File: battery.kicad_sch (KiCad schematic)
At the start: 1 part, among them J2 Screw_Terminal_01x02

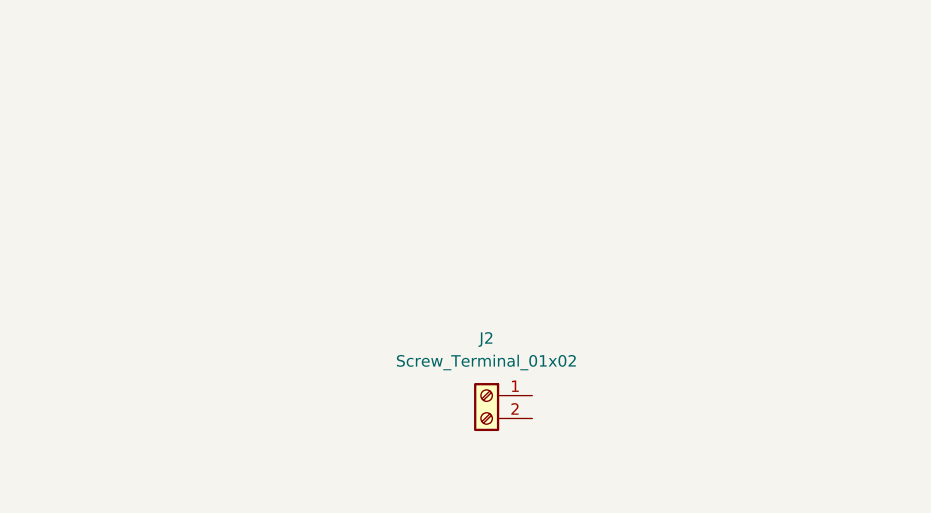
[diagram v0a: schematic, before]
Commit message: Started working on the audio input, including a rough-draft of the first stage.
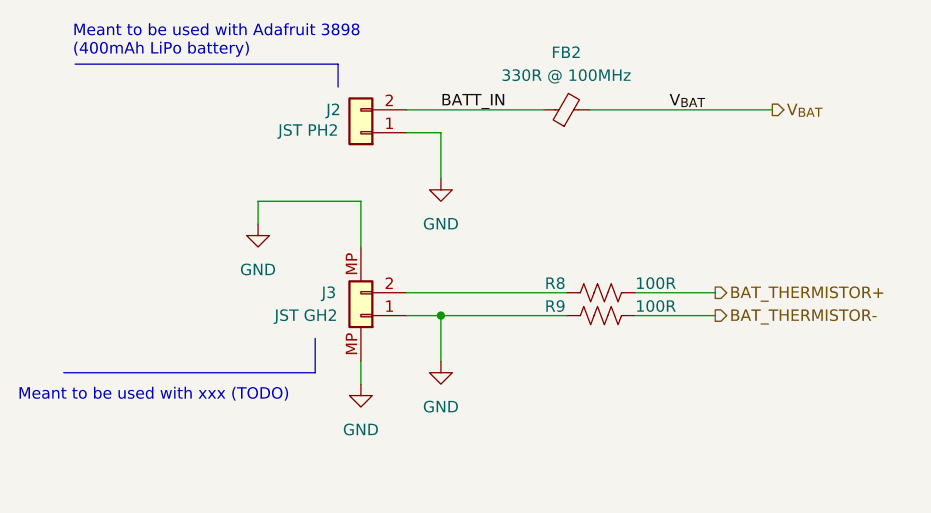
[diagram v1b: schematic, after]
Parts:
- removed J2: Screw_Terminal_01x02, Connector_JST:JST_PH_S2B-PH-SM4-TB_1x02-1MP_P2.00mm_Horizontal, symbol Connector:Screw_Terminal_01x02
- added FB2: 330R @ 100MHz, Inductor_SMD:L_0402_1005Metric, symbol #inventree_kicad:FB_330R_0402_1A2
- added J2: JST PH2, Connector_JST:JST_PH_S2B-PH-K_1x02_P2.00mm_Horizontal, symbol #inventree_kicad:PWR_CONN_2PIN_JST_PH2_RA_THRU
- added J3: JST GH2, Connector_JST:JST_GH_SM02B-GHS-TB_1x02-1MP_P1.25mm_Horizontal, symbol #inventree_kicad:SIG_CONN_2PIN_JST_GH2_RA_SMD
- added R8, R9: 100R, Resistor_SMD:R_0402_1005Metric, symbol #inventree_kicad:R_100R_0402_1PCT_0W0625
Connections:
- new net: J3.2 (Pin_2), R8.1
- new net BATT_IN: FB2.1, J2.2 (Pin_2)
- new net BAT_THERMISTOR+: R8.2
- new net BAT_THERMISTOR-: R9.2
- new net GND: J2.1 (Pin_1), J3.1 (Pin_1), J3.MP, R9.1
- new net V_{BAT}: FB2.2
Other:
- note added: "Meant to be used with Adafruit 3898 (400mAh LiPo battery)"
- note added: "Meant to be used with xxx (TODO)"

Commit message: Implemented boost stage and now working on schematics for current buffers and rail splitter.
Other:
- title: (none) -> ${PROJECT_NAME}
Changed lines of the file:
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@@
 	(generator_version "10.0")
 	(paper "A4")
+	(title_block
+		(title "${PROJECT_NAME}")
+		(date "2026-08-25")
+		(rev "${REVISION}")
+		(comment 1 "${PCBA_IPN}")
+	)
 	(text "Meant to be used with xxx (TODO)"
 		(exclude_from_sim no)

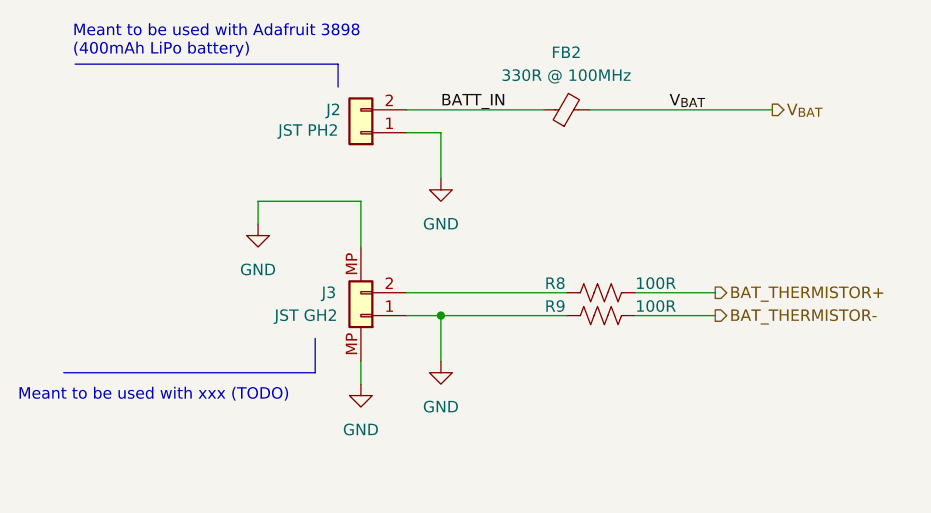
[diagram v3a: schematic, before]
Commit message: Preliminary layout complete, done on airpane so needs verification.
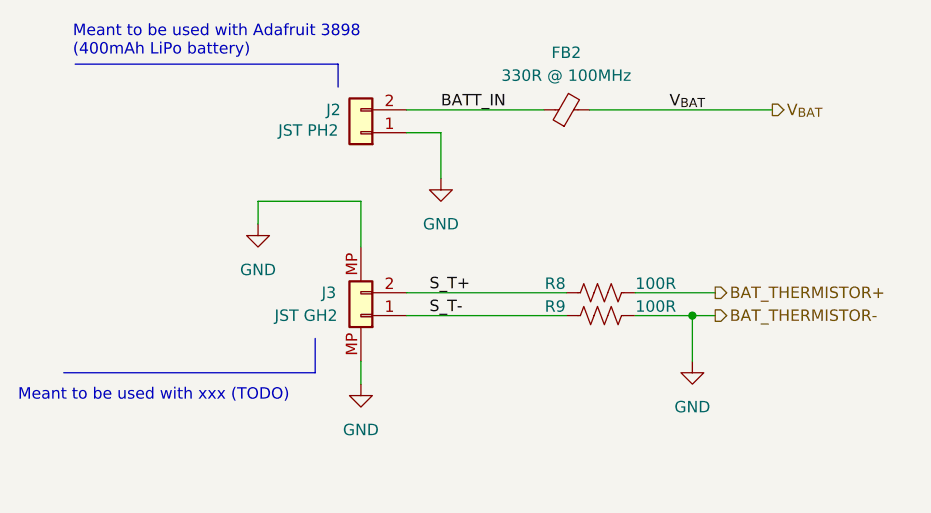
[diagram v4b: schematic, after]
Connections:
- net BAT_THERMISTOR- is gone; now on net GND: R9.2
- net GND: no longer J3.1 (Pin_1), R9.1
- net S_T+: now reaches J3.2 (Pin_2), R8.1
- new net S_T-: J3.1 (Pin_1), R9.1
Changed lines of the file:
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@@
 	)
 	(junction
-		(at 72.39 99.06)
+		(at 100.33 99.06)
 		(diameter 0)
 		(color 0 0 0 0)
@@
 	(wire
 		(pts
-			(xy 72.39 99.06) (xy 72.39 104.14)
-		)
-		(stroke
-			(width 0)
-			(type default)
-		)
-	)
-	(wire
-		(pts
 			(xy 52.07 88.9) (xy 52.07 86.36)
 		)
@@
 	(wire
 		(pts
-			(xy 93.98 99.06) (xy 102.87 99.06)
+			(xy 93.98 99.06) (xy 100.33 99.06)
 		)
 		(stroke
@@
 	(wire
 		(pts
-			(xy 68.58 99.06) (xy 72.39 99.06)
+			(xy 100.33 99.06) (xy 100.33 104.14)
+		)
+		(stroke
+			(width 0)
+			(type default)
+		)
+	)
+	(wire
+		(pts
+			(xy 68.58 99.06) (xy 86.36 99.06)
 		)
 		(stroke
@@
 	(wire
 		(pts
-			(xy 72.39 99.06) (xy 86.36 99.06)
-		)
-		(stroke
-			(width 0)
-			(type default)
-		)
-	)
-	(wire
-		(pts
 			(xy 63.5 104.14) (xy 63.5 106.68)
+		)
+		(stroke
+			(width 0)
+			(type default)
+		)
+	)
+	(wire
+		(pts
+			(xy 100.33 99.06) (xy 102.87 99.06)
 		)
 		(stroke
@@
 	(label "BATT_IN"
 		(at 72.39 76.2 0)
+		(effects
+			(font
+				(size 1.27 1.27)
+			)
+			(justify left bottom)
+		)
+	)
+	(label "S_T-"
+		(at 71.12 99.06 0)
+		(effects
+			(font
+				(size 1.27 1.27)
+			)
+			(justify left bottom)
+		)
+	)
+	(label "S_T+"
+		(at 71.12 96.52 0)
 		(effects
 			(font
@@
 	)
 	(symbol
-		(lib_id "power:GND")
-		(at 72.39 104.14 0)
-		(unit 1)
-		(body_style 1)
-		(exclude_from_sim no)
-		(in_bom yes)
-		(on_board yes)
-		(in_pos_files yes)
-		(dnp no)
-		(fields_autoplaced yes)
-		(property "Reference" "#PWR014"
-			(at 72.39 110.49 0)
-			(hide yes)
-			(show_name no)
-			(do_not_autoplace no)
-			(effects
-				(font
-					(size 1.27 1.27)
-				)
-			)
-		)
-		(property "Value" "GND"
-			(at 72.39 109.22 0)
-			(show_name no)
-			(do_not_autoplace no)
-			(effects
-				(font
-					(size 1.27 1.27)
-				)
-			)
-		)
-		(property "Footprint" ""
-			(at 72.39 104.14 0)
-			(hide yes)
-			(show_name no)
-			(do_not_autoplace no)
-			(effects
-				(font
-					(size 1.27 1.27)
-				)
-			)
-		)
-		(property "Datasheet" ""
-			(at 72.39 104.14 0)
-			(hide yes)
-			(show_name no)
-			(do_not_autoplace no)
-			(effects
-				(font
-					(size 1.27 1.27)
-				)
-			)
-		)
-		(property "Description" "Power symbol creates a global label with name \"GND\" , ground"
-			(at 72.39 104.14 0)
-			(hide yes)
-			(show_name no)
-			(do_not_autoplace no)
-			(effects
-				(font
-					(size 1.27 1.27)
-				)
-			)
-		)
-		(pin "1"
-		)
-		(instances
-			(project "headphone_amp"
-				(path "/62ffec33-ae93-49a8-bfe6-566578dd8e82/74a7e50f-a1a3-4295-a28c-ad733432c5cd"
-					(reference "#PWR014")
-					(unit 1)
-				)
-			)
-		)
-	)
-	(symbol
 		(lib_id "#inventree_kicad:FB_330R_0402_1A2")
 		(at 86.36 76.2 90)
@@
 					(unit 1)
 				)
+			)
+		)
+	)
+	(symbol
+		(lib_id "power:GND")
+		(at 100.33 104.14 0)
+		(unit 1)
+		(body_style 1)
+		(exclude_from_sim no)
+		(in_bom yes)
+		(on_board yes)
+		(in_pos_files yes)
+		(dnp no)
+		(fields_autoplaced yes)
+		(property "Reference" "#PWR014"
+			(at 100.33 110.49 0)
+			(hide yes)
+			(show_name no)
+			(do_not_autoplace no)
+			(effects
+				(font
+					(size 1.27 1.27)
+				)
+			)
+		)
+		(property "Value" "GND"
+			(at 100.33 109.22 0)
+			(show_name no)
+			(do_not_autoplace no)
+			(effects
+				(font
+					(size 1.27 1.27)
+				)
+			)
+		)
+		(property "Footprint" ""
+			(at 100.33 104.14 0)
+			(hide yes)
+			(show_name no)
+			(do_not_autoplace no)
+			(effects
+				(font
+					(size 1.27 1.27)
+				)
+			)
+		)
+		(property "Datasheet" ""
+			(at 100.33 104.14 0)
+			(hide yes)
+			(show_name no)
+			(do_not_autoplace no)
+			(effects
+				(font
+					(size 1.27 1.27)
+				)
+			)
+		)
+		(property "Description" "Power symbol creates a global label with name \"GND\" , ground"
+			(at 100.33 104.14 0)
+			(hide yes)
+			(show_name no)
+			(do_not_autoplace no)
+			(effects
+				(font
+					(size 1.27 1.27)
+				)
+			)
+		)
+		(pin "1"
+		)
+		(instances
+			(project "headphone_amp"
+				(path "/62ffec33-ae93-49a8-bfe6-566578dd8e82/74a7e50f-a1a3-4295-a28c-ad733432c5cd"
+					(reference "#PWR014")
+					(unit 1)
+				)

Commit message: Picked off the board parts and ordered on DigiKey -- also added notes on schematic.
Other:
- note added: "Meant to be used with B57861S0103F040"
- note removed: "Meant to be used with xxx (TODO)"
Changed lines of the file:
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@@
 		(comment 1 "${PCBA_IPN}")
 	)
-	(text "Meant to be used with xxx (TODO)"
+	(text "Meant to be used with B57861S0103F040"
 		(exclude_from_sim no)
-		(at 25.4 107.95 0)
+		(at 26.162 117.856 0)
 		(effects
 			(font
@@
 	(polyline
 		(pts
-			(xy 30.48 105.41) (xy 58.42 105.41)
+			(xy 26.67 115.57) (xy 58.42 115.57)
 		)
 		(stroke
@@
 	(polyline
 		(pts
-			(xy 58.42 101.6) (xy 58.42 105.41)
+			(xy 58.42 101.6) (xy 58.42 115.57)
 		)
 		(stroke

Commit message: Finally updated all parts in InvenTree and linked them with KiCAD. Ready for BOM exports to JLC.
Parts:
- R8, R9: symbol #inventree_kicad:R_100R_0402_1PCT_0W0625 -> inventree_kicad:R_100R_0402_1PCT_0W0625
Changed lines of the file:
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@@
 	)
 	(symbol
-		(lib_id "#inventree_kicad:R_100R_0402_1PCT_0W0625")
+		(lib_id "inventree_kicad:R_100R_0402_1PCT_0W0625")
 		(at 90.17 96.52 90)
 		(unit 1)
@@
 	)
 	(symbol
-		(lib_id "#inventree_kicad:R_100R_0402_1PCT_0W0625")
+		(lib_id "inventree_kicad:R_100R_0402_1PCT_0W0625")
 		(at 90.17 99.06 90)
 		(unit 1)
